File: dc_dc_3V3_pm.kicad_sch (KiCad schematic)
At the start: 15 parts, among them U15 TPS56339DDC

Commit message: corrected LCSC for 4.7uH inductors
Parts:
- L4: LCSC Part C167220 -> C167230
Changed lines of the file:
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@@
       (effects (font (size 1.27 1.27)) hide)
     )
-    (property "Datasheet" "https://datasheet.lcsc.com/lcsc/1811132109_cjiang-Changjiang-Microelectronics-Tech-FXL0630-4R7-M_C167220.pdf" (id 3) (at 168.275 98.425 0)
+    (property "Datasheet" "https://datasheet.lcsc.com/lcsc/1806150431_cjiang--Changjiang-Microelectronics-Tech-FXL1040-4R7-M_C167230.pdf" (id 3) (at 168.275 98.425 0)
       (effects (font (size 1.27 1.27)) hide)
     )
-    (property "LCSC Part" "C167220" (id 4) (at 168.275 98.425 90)
+    (property "LCSC Part" "C167230" (id 4) (at 168.275 98.425 90)
       (effects (font (size 1.27 1.27)) hide)
     )

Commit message: corrected LCSC of 22uF caps
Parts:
- C66, C67: LCSC Part C49217 -> C12891
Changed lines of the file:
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@@
       (effects (font (size 1.27 1.27)) hide)
     )
-    (property "LCSC Part" "C49217" (id 4) (at 186.055 99.695 0)
+    (property "LCSC Part" "C12891" (id 4) (at 186.055 99.695 0)
       (effects (font (size 1.27 1.27)) hide)
     )
@@
       (effects (font (size 1.27 1.27)) hide)
     )
-    (property "LCSC Part" "C49217" (id 4) (at 197.485 99.695 0)
+    (property "LCSC Part" "C12891" (id 4) (at 197.485 99.695 0)
       (effects (font (size 1.27 1.27)) hide)
     )

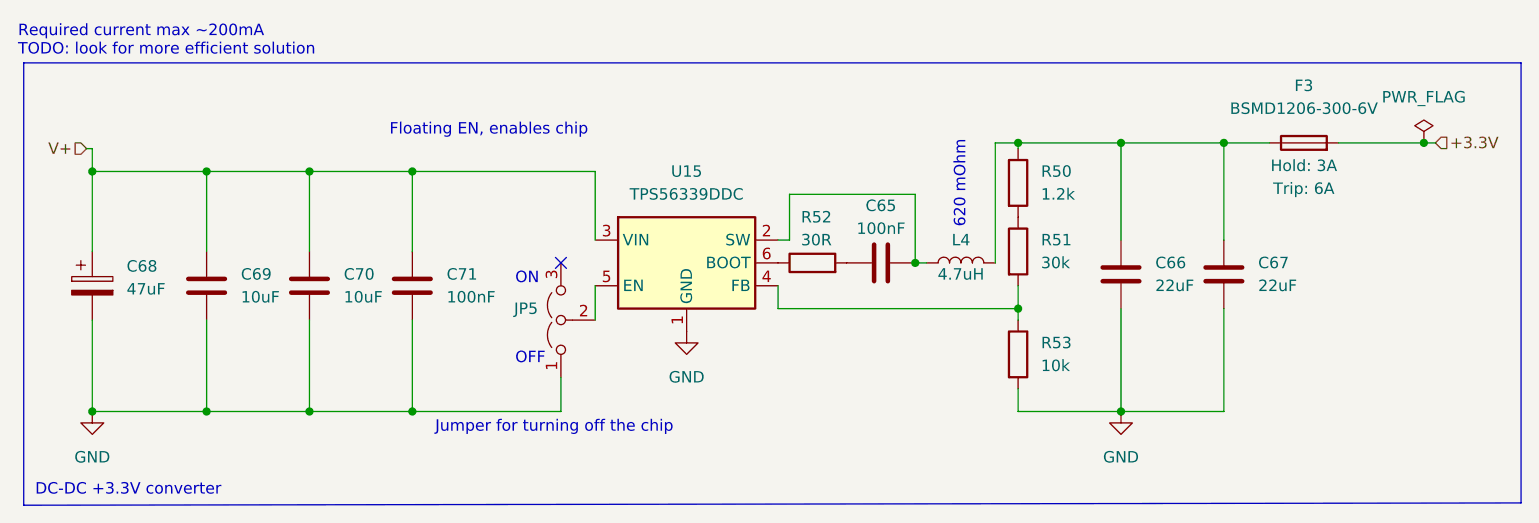
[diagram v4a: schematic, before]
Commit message: Power circuit initial routing
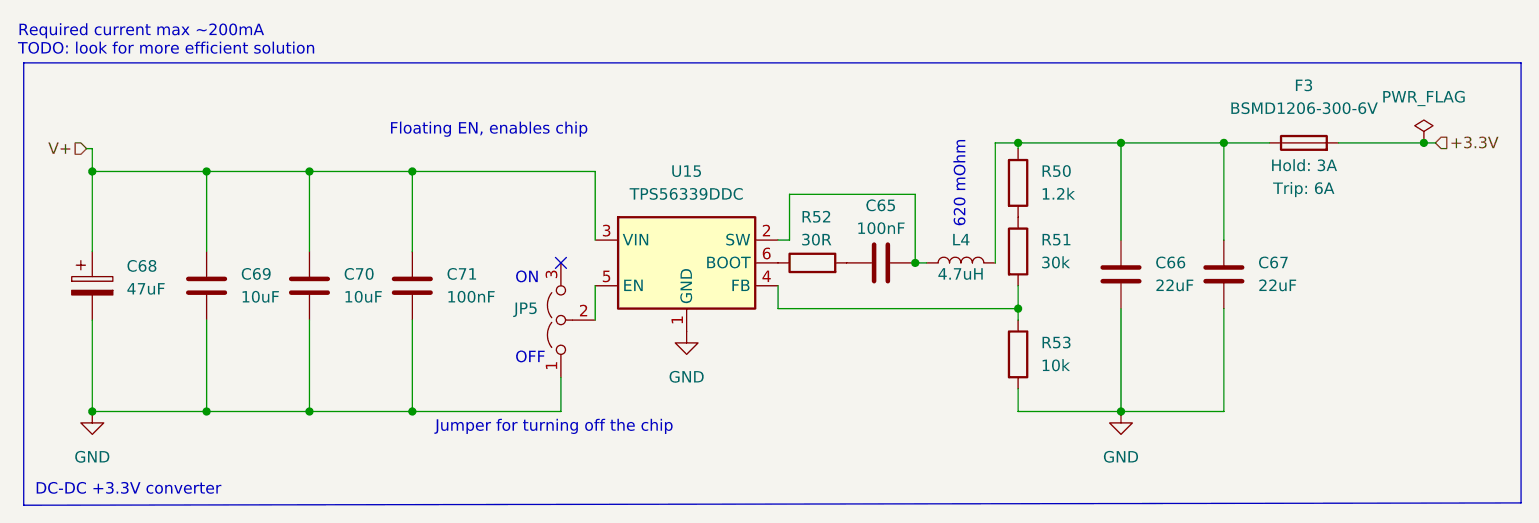
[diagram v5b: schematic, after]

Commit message: replaced 47uF caps due to supply shortage, rotation fix for 3535 adressable leds
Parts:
- C68: LCSC Part C403725 -> C76659
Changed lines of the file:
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@@
       (effects (font (size 1.27 1.27)) hide)
     )
-    (property "Datasheet" "https://datasheet.lcsc.com/lcsc/1912111437_Murata-Electronics-GRM31CR61E476ME44L_C403725.pdf" (at 71.755 100.965 0)
+    (property "Datasheet" "https://datasheet.lcsc.com/lcsc/2304140030_TDK-C3216X5R1E476MTJ00E_C76659.pdf" (at 71.755 100.965 0)
       (effects (font (size 1.27 1.27)) hide)
     )
@@
       (effects (font (size 1.27 1.27)) hide)
     )
-    (property "LCSC Part" "C403725" (at 71.755 100.965 0)
+    (property "LCSC Part" "C76659" (at 71.755 100.965 0)
       (effects (font (size 1.27 1.27)) hide)
     )

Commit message: updated drawing corner, added license
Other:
- company: (none) -> University of Tartu
- title: (none) -> DC-DC converter for the power management subsystem
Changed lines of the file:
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@@
 (kicad_sch (version 20230121) (generator eeschema)
   (paper "A4")
+  (title_block
+    (title "DC-DC converter for the power management subsystem")
+    (date "2023-21-11")
+    (rev "0.2.0")
+    (company "University of Tartu")
+    (comment 1 "Licensed under CERN-OHL-P")
+  )
   (junction (at 71.755 88.265) (diameter 0) (color 0 0 0 0)
   )
